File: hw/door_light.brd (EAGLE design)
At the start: 32.2 x 34.6 mm, 28 parts, among them IC1 TINY13-20SSU, Q1 BSP250, T2 KP-3216P3C, U1 MC33063ADE4

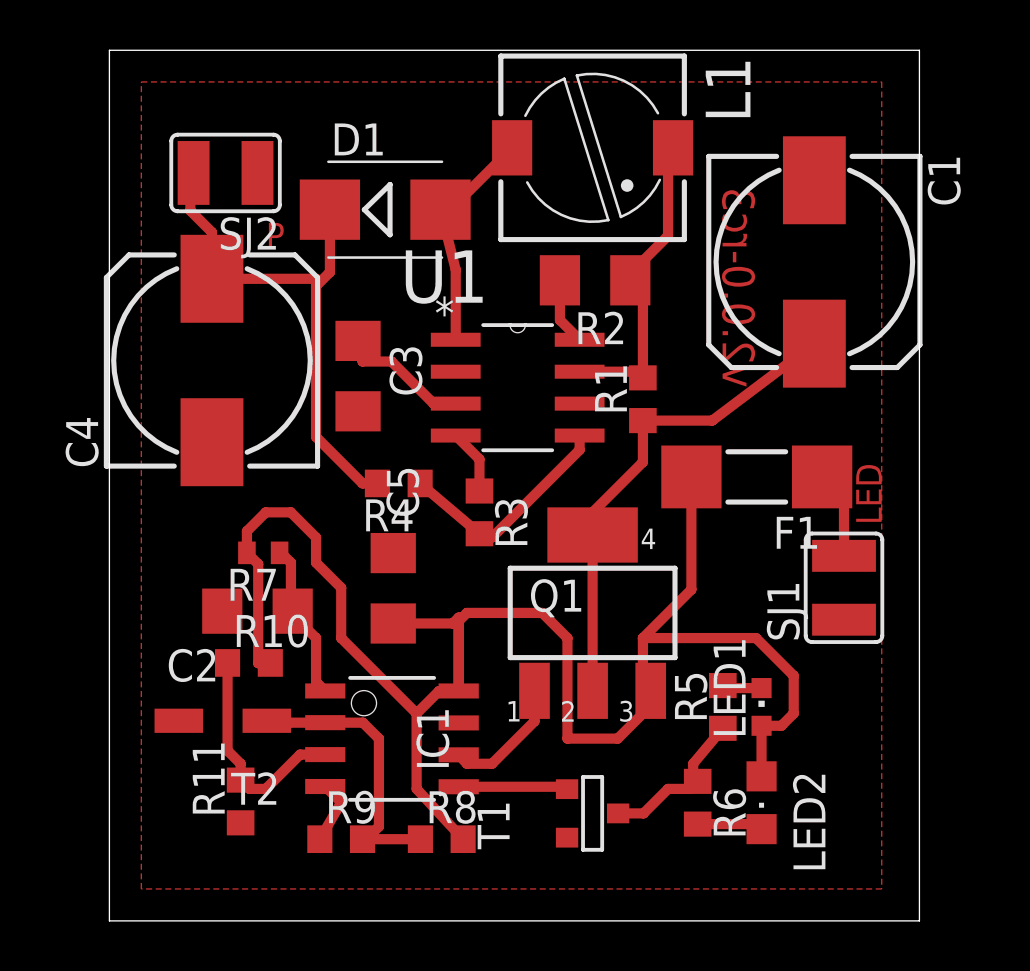
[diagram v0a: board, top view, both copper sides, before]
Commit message: fixed IR led size (was 805, should be 1206)
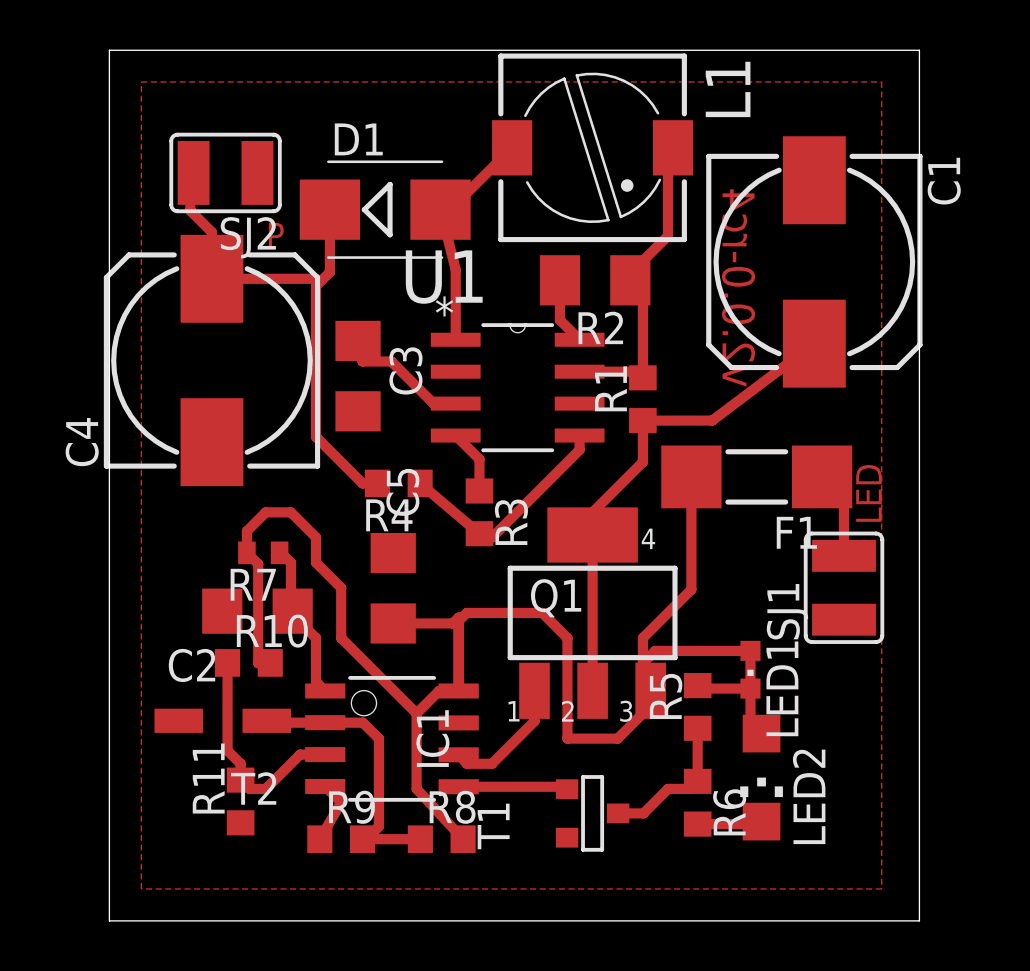
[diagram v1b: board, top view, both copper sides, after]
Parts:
- LED2: device led:CHIPLED_0805 -> led:CHIPLED_1206
- T1: value (none) -> n-mosfet
- moved LED1 1.54 mm to (43.3, 49.7), turned to 180 degrees
- moved LED2 1.00 mm to (43.7, 45.5)
- moved R5 1.00 mm to (41.2, 48.3)
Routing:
- net +4.1V: track 68.8 -> 65.2 mm
- net N$1: track 1.58 -> 2.15 mm
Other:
- board text added: "v2.0.0-rc4"
- board text removed: "v2.0.0-rc3"
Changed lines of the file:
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@@
 <layer number="23" name="tOrigins" color="15" fill="1" visible="yes" active="yes"/>
 <layer number="24" name="bOrigins" color="15" fill="1" visible="yes" active="yes"/>
-<layer number="25" name="tNames" color="7" fill="1" visible="no" active="yes"/>
-<layer number="26" name="bNames" color="7" fill="1" visible="no" active="yes"/>
-<layer number="27" name="tValues" color="7" fill="1" visible="no" active="yes"/>
-<layer number="28" name="bValues" color="7" fill="1" visible="no" active="yes"/>
+<layer number="25" name="tNames" color="7" fill="1" visible="yes" active="yes"/>
+<layer number="26" name="bNames" color="7" fill="1" visible="yes" active="yes"/>
+<layer number="27" name="tValues" color="7" fill="1" visible="yes" active="yes"/>
+<layer number="28" name="bValues" color="7" fill="1" visible="yes" active="yes"/>
 <layer number="29" name="tStop" color="7" fill="3" visible="no" active="yes"/>
 <layer number="30" name="bStop" color="7" fill="6" visible="no" active="yes"/>
@@
 <wire x1="50" y1="74.38" x2="17.78" y2="74.38" width="0" layer="20"/>
 <wire x1="17.78" y1="74.38" x2="17.78" y2="39.75" width="0" layer="20"/>
-<text x="43.44" y="68.94" size="1.27" layer="1" rot="MR270">v2.0.0-rc3</text>
+<text x="43.44" y="68.94" size="1.27" layer="1" rot="MR270">v2.0.0-rc4</text>
 <text x="24" y="66.5" size="1.016" layer="1">P</text>
 <text x="48.5" y="55.5" size="1.016" layer="1" rot="R90">LED</text>
@@
 <element name="R8" library="rcl" package="R0603" value="10kR" x="31" y="43"/>
 <element name="R11" library="rcl" package="R0603" value="2.9kR" x="23" y="44.5" rot="R90"/>
-<element name="LED2" library="led" package="CHIPLED_0805" value="IR" x="43.72" y="44.45" rot="R180"/>
-<element name="LED1" library="led" package="CHIPLED_0603" value="RED" x="43.72" y="48.26"/>
+<element name="LED2" library="led" package="CHIPLED_1206" value="IR" x="43.72" y="45.45" rot="R180"/>
+<element name="LED1" library="led" package="CHIPLED_0603" value="RED" x="43.28" y="49.74" rot="R180"/>
 <element name="R6" library="rcl" package="R0603" value="470R" x="41.18" y="44.45" rot="R270"/>
-<element name="R5" library="rcl" package="R0603" value="470R" x="42.18" y="48.26" rot="R90"/>
+<element name="R5" library="rcl" package="R0603" value="470R" x="41.18" y="48.26" rot="R90"/>
 <element name="T2" library="opto-trans-smd" package="OPTO-TRANS-SIEMENS_BP103" value="KP-3216P3C" x="22.67" y="48.18" rot="R180">
 <attribute name="OC_NEWARK" value="unknown" x="22.67" y="48.18" size="1.778" layer="27" rot="R180" display="off"/>
@@
 </element>
 <element name="Q1" library="transistor-fet" package="SOT223" value="BSP250" x="37" y="52"/>
-<element name="T1" library="zetex" package="SOT-23" value="" x="37" y="44" rot="R90">
+<element name="T1" library="zetex" package="SOT-23" value="n-mosfet" x="37" y="44" rot="R90">
 <attribute name="OC_NEWARK" value="unknown" x="37" y="44" size="1.778" layer="27" rot="R90" display="off"/>
 <attribute name="MPN" value="" x="37" y="44" size="1.778" layer="27" rot="R90" display="off"/>
@@
 <contactref element="R6" pad="2"/>
 <wire x1="41.18" y1="43.6" x2="43.52" y2="43.6" width="0.4064" layer="1"/>
-<wire x1="43.52" y1="43.6" x2="43.72" y2="43.4" width="0.4064" layer="1"/>
+<wire x1="43.52" y1="43.6" x2="43.72" y2="43.7" width="0.4064" layer="1"/>
 </signal>
 <signal name="N$4">
@@
 <wire x1="40.88" y1="45" x2="41.18" y2="45.3" width="0.4064" layer="1"/>
 <wire x1="41.18" y1="45.3" x2="41" y2="45.3" width="0.4064" layer="1"/>
-<wire x1="41" y1="45.3" x2="41" y2="46" width="0.4064" layer="1"/>
-<wire x1="41" y1="46" x2="42.18" y2="47.41" width="0.4064" layer="1"/>
+<wire x1="41.18" y1="45.3" x2="41.18" y2="47.41" width="0.4064" layer="1"/>
 </signal>
 <signal name="N$9">
@@
 <contactref element="Q1" pad="3"/>
 <wire x1="31.674" y1="48.895" x2="31.674" y2="51.816" width="0.4064" layer="1"/>
-<wire x1="43.72" y1="45.5" x2="43.72" y2="47.51" width="0.4064" layer="1"/>
 <wire x1="40.93" y1="57.41" x2="40.93" y2="52.93" width="0.4064" layer="1"/>
 <wire x1="40.93" y1="52.93" x2="39" y2="51" width="0.4064" layer="1"/>
-<wire x1="39" y1="51" x2="39" y2="49.2126" width="0.4064" layer="1"/>
+<wire x1="39" y1="51" x2="39" y2="50" width="0.4064" layer="1"/>
+<wire x1="39" y1="50" x2="39" y2="49.2126" width="0.4064" layer="1"/>
 <wire x1="39" y1="49.2126" x2="39.3114" y2="48.9012" width="0.4064" layer="1"/>
 <wire x1="31.674" y1="48.895" x2="31.674" y2="51.674" width="0.4064" layer="1"/>
@@
 <wire x1="24.18" y1="49.82" x2="23.7" y2="50" width="0.4064" layer="1"/>
 <wire x1="23.7" y1="50" x2="23.7" y2="53.94" width="0.4064" layer="1"/>
-<wire x1="43.72" y1="47.51" x2="44.51" y2="47.51" width="0.4064" layer="1"/>
-<wire x1="44.51" y1="47.51" x2="45" y2="48" width="0.4064" layer="1"/>
-<wire x1="45" y1="48" x2="45" y2="49.5" width="0.4064" layer="1"/>
-<wire x1="45" y1="49.5" x2="43.5" y2="51" width="0.4064" layer="1"/>
-<wire x1="43.5" y1="51" x2="39" y2="51" width="0.4064" layer="1"/>
 <wire x1="32" y1="52" x2="35" y2="52" width="0.4064" layer="1"/>
 <wire x1="35" y1="52" x2="36" y2="51" width="0.4064" layer="1"/>
@@
 <wire x1="29.07" y1="51.58" x2="31.438" y2="51.58" width="0.4064" layer="1"/>
 <wire x1="31.438" y1="51.58" x2="31.674" y2="51.816" width="0.4064" layer="1"/>
+<wire x1="43.28" y1="50.49" x2="39.49" y2="50.49" width="0.4064" layer="1"/>
+<wire x1="39.49" y1="50.49" x2="39" y2="50" width="0.4064" layer="1"/>
+<wire x1="43.28" y1="50.49" x2="43.28" y2="47.64" width="0.4064" layer="1"/>
+<wire x1="43.28" y1="47.64" x2="43.72" y2="47.2" width="0.4064" layer="1"/>
 </signal>
 <signal name="N$10">
@@
 <contactref element="LED1" pad="C"/>
 <contactref element="R5" pad="2"/>
-<wire x1="43.72" y1="49.01" x2="42.28" y2="49.01" width="0.4064" layer="1"/>
-<wire x1="42.28" y1="49.01" x2="42.18" y2="49.11" width="0.4064" layer="1"/>
+<wire x1="43.28" y1="48.99" x2="41.3" y2="48.99" width="0.4064" layer="1"/>
+<wire x1="41.3" y1="48.99" x2="41.18" y2="49.11" width="0.4064" layer="1"/>
 </signal>
 <signal name="N$14">

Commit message: replaced fuse with the one of a proper type and size (1812)
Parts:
- F1: value 1206L035YR (F750mA) -> SD075-16 (F750mA)
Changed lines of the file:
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@@
 <layer number="23" name="tOrigins" color="15" fill="1" visible="yes" active="yes"/>
 <layer number="24" name="bOrigins" color="15" fill="1" visible="yes" active="yes"/>
-<layer number="25" name="tNames" color="7" fill="1" visible="yes" active="yes"/>
-<layer number="26" name="bNames" color="7" fill="1" visible="yes" active="yes"/>
-<layer number="27" name="tValues" color="7" fill="1" visible="yes" active="yes"/>
-<layer number="28" name="bValues" color="7" fill="1" visible="yes" active="yes"/>
+<layer number="25" name="tNames" color="7" fill="1" visible="no" active="yes"/>
+<layer number="26" name="bNames" color="7" fill="1" visible="no" active="yes"/>
+<layer number="27" name="tValues" color="7" fill="1" visible="no" active="yes"/>
+<layer number="28" name="bValues" color="7" fill="1" visible="no" active="yes"/>
 <layer number="29" name="tStop" color="7" fill="3" visible="no" active="yes"/>
 <layer number="30" name="bStop" color="7" fill="6" visible="no" active="yes"/>
@@
 <attribute name="OC_FARNELL" value="1053588" x="34.02" y="60.96" size="1.778" layer="27" display="off"/>
 </element>
-<element name="F1" library="rcl" package="MINI_MELF-0207W" value="1206L035YR (F750mA)" x="43.53" y="57.41" rot="R180"/>
+<element name="F1" library="rcl" package="MINI_MELF-0207W" value="SD075-16 (F750mA)" x="43.53" y="57.41" rot="R180"/>
 <element name="R7" library="rcl" package="R0402" value="10kR" x="23.9" y="54.39" rot="R180"/>
 <element name="D1" library="diode" package="SMB" value=" MBRS140T3G" x="28.75" y="68.04"/>
